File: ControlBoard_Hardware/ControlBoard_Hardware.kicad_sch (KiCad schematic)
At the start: 20 parts, among them U2 TSR_1-2450

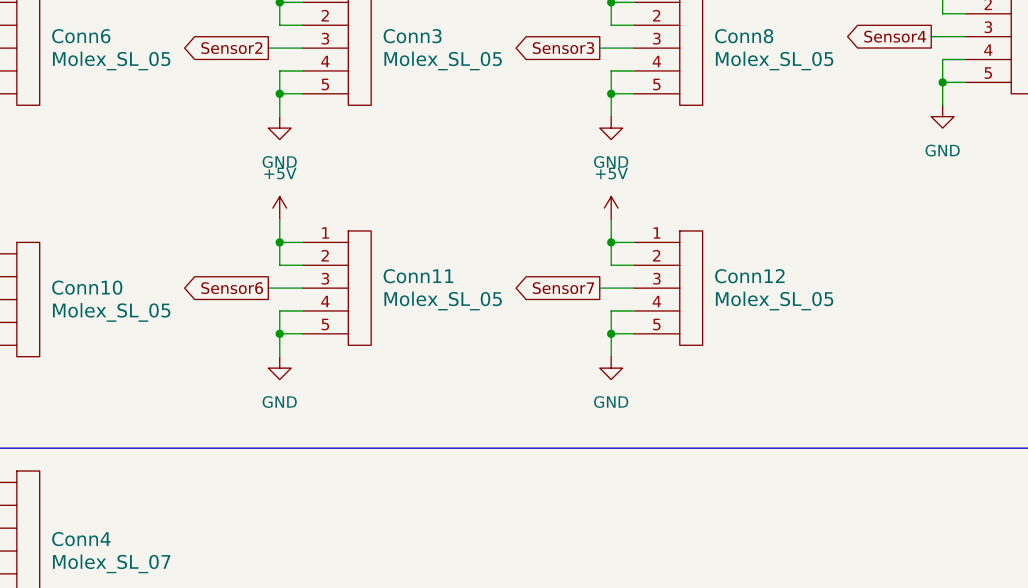
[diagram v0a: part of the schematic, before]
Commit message: Assigned footprints
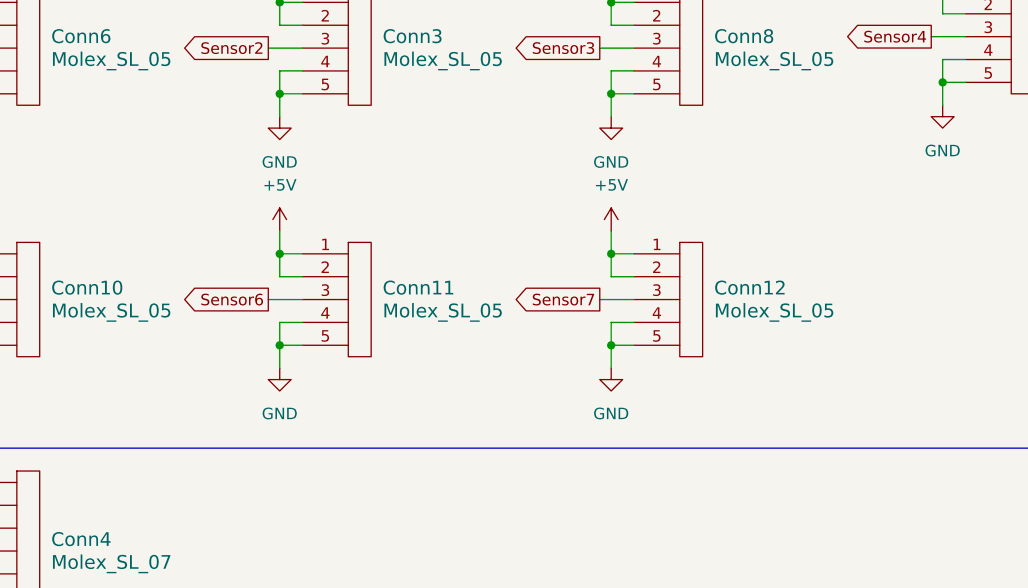
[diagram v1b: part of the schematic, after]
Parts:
- Conn1, Conn7: footprint (none) -> MRDT_Connectors:MOLEX_SL_02_Horizontal
- Conn10, Conn11, Conn12, Conn3, Conn6, Conn8, Conn9: footprint (none) -> MRDT_Connectors:MOLEX_SL_05_Vertical
- Conn2: footprint (none) -> MRDT_Connectors:MOLEX_SL_04_Horizontal
- Conn4, Conn5: footprint (none) -> MRDT_Connectors:MOLEX_SL_07_Horizontal
- D1, D2, D3: footprint (none) -> LED_SMD:LED_0201_0603Metric_Pad0.64x0.40mm_HandSolder
- R1, R2, R3: footprint (none) -> Resistor_SMD:R_0603_1608Metric_Pad0.98x0.95mm_HandSolder
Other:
- moved on the sheet: Conn11, Conn12

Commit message: Revert "Assigned footprints"
This reverts commit 6f2e1c40c0d01355b4ad57b50ebbed6eef59f7aa.
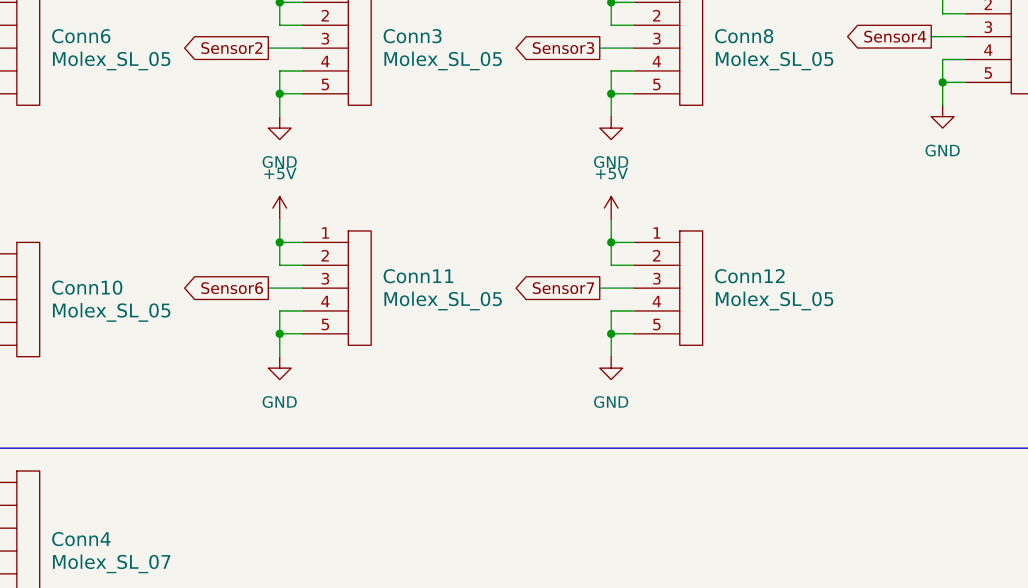
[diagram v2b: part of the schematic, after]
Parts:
- Conn1, Conn7: footprint MRDT_Connectors:MOLEX_SL_02_Horizontal -> (none)
- Conn10, Conn11, Conn12, Conn3, Conn6, Conn8, Conn9: footprint MRDT_Connectors:MOLEX_SL_05_Vertical -> (none)
- Conn2: footprint MRDT_Connectors:MOLEX_SL_04_Horizontal -> (none)
- Conn4, Conn5: footprint MRDT_Connectors:MOLEX_SL_07_Horizontal -> (none)
- D1, D2, D3: footprint LED_SMD:LED_0201_0603Metric_Pad0.64x0.40mm_HandSolder -> (none)
- R1, R2, R3: footprint Resistor_SMD:R_0603_1608Metric_Pad0.98x0.95mm_HandSolder -> (none)
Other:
- moved on the sheet: Conn11, Conn12

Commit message: Made layout
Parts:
- added H1, H2, H3, H4: MountingHole, MRDT_Drill_Holes:4_40_Hole_Corner, symbol Mechanical:MountingHole
- Conn1, Conn7: footprint (none) -> MRDT_Connectors:MOLEX_SL_02_Horizontal
- Conn10, Conn11, Conn12, Conn3, Conn6, Conn8, Conn9: footprint (none) -> MRDT_Connectors:MOLEX_SL_05_Horizontal
- Conn2: footprint (none) -> MRDT_Connectors:MOLEX_SL_04_Horizontal
- Conn4, Conn5: footprint (none) -> MRDT_Connectors:MOLEX_SL_07_Horizontal
- D1, D2, D3: footprint (none) -> LED_SMD:LED_0603_1608Metric_Pad1.05x0.95mm_HandSolder
- R1, R2, R3: footprint (none) -> Resistor_SMD:R_0603_1608Metric_Pad0.98x0.95mm_HandSolder
- U1: footprint (none) -> ControlBoard_Footprints:Teensy_4_0
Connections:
- net DIscharge7 is gone; now on net Discharge7: Conn5.7
- net Charge1: now also U1.13 (SCK); no longer U1.2 (OUT2)
- net Charge2: now also U1.14 (A0); no longer U1.4 (BCLK2)
- net Charge3: now also U1.15 (A1); no longer U1.6 (OUT1D)
- net Charge4: now also U1.16 (A2); no longer U1.8 (TX2)
- net Charge5: now also U1.2 (OUT2); no longer U1.10 (CS)
- net Charge6: now also U1.3 (LRCLK2); no longer U1.16 (A2)
- net Charge7: now also U1.4 (BCLK2); no longer U1.14 (A0)
- net Discharge1: now also U1.5 (IN2); no longer U1.3 (LRCLK2)
- net Discharge2: now also U1.6 (OUT1D); no longer U1.5 (IN2)
- net Discharge4: now also U1.8 (TX2); no longer U1.9 (OUT1C)
- net Discharge5: now also U1.9 (OUT1C); no longer U1.11 (MOSI)
- net Discharge6: now also U1.10 (CS); no longer U1.15 (A1)
- net Discharge7: now also U1.11 (MOSI); no longer U1.13 (SCK)

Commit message: updatedfor final report
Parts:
- removed Conn4, Conn5: Molex_SL_07, MRDT_Connectors:MOLEX_SL_07_Horizontal, symbol MRDT_Connectors:Molex_SL_07
- added Conn13, Conn4: Molex_SL_02, MRDT_Connectors:MOLEX_SL_02_Horizontal, symbol MRDT_Connectors:Molex_SL_02
- added Conn5: Molex_SL_03, MRDT_Connectors:MOLEX_SL_03_Horizontal, symbol MRDT_Connectors:Molex_SL_03
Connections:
- net +3V3: now also Conn10.1, Conn10.2, Conn11.1, Conn11.2, Conn12.1, Conn12.2, Conn3.1, Conn3.2, Conn6.1, Conn6.2, Conn8.1, Conn8.2, Conn9.1, Conn9.2; no longer Conn7.1
- net +5V: now also Conn5.1; no longer Conn10.1, Conn10.2, Conn11.1, Conn11.2, Conn12.1, Conn12.2, Conn3.1, Conn3.2, Conn6.1, Conn6.2, Conn8.1, Conn8.2, Conn9.1, Conn9.2
- net Charge1: now also Conn4.1
- net Discharge1: now also Conn4.2
- net GND: now also Conn7.2, Conn13.2, Conn5.3
- net Trigger Signal: now also Conn7.1; no longer Conn7.2
- net Charge2: no longer names the net of U1.14 (A0)
- net Charge3: no longer names the net of U1.15 (A1)
- net Charge4: no longer names the net of U1.16 (A2)
- net Charge5: no longer names the net of U1.2 (OUT2)
- net Charge6: no longer names the net of U1.3 (LRCLK2)
- net Charge7: no longer names the net of U1.4 (BCLK2)
- net Discharge2 renamed SERVO
- net SERVO: now also Conn5.2
- net Discharge3: no longer names the net of U1.7 (RX2)
- net Discharge4: no longer names the net of U1.8 (TX2)
- net Discharge5: no longer names the net of U1.9 (OUT1C)
- net Discharge6: no longer names the net of U1.10 (CS)
- net Discharge7: no longer names the net of U1.11 (MOSI)
- new net Safety Switch: Conn13.1
- no-connect marks 0 -> 11
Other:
- note added: "Charging/Discharging Circuits"
- note added: "Safety Switch"
- note removed: "Charging Circuits"
- note removed: "Discharging Circuits"
- moved on the sheet: Conn7
